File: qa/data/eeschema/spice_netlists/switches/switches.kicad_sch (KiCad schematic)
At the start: 8 parts, among them K1 ADW11

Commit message: Sim: Implement "enum" model parameters for switches
Displayed in Sim Model Dialog parameter grid as a dropdown
(wxEnumProperty).
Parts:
- K1: Sim_Params thr=500m his=0 ron=100m roff=1T ic=on -> thr=500m his=0 ron=100m roff=1T
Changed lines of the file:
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@@
       (effects (font (size 1.27 1.27)) hide)
     )
-    (property "Sim_Params" "thr=500m his=0 ron=100m roff=1T ic=on" (id 7) (at 163.83 83.82 0)
+    (property "Sim_Params" "thr=500m his=0 ron=100m roff=1T" (id 7) (at 163.83 83.82 0)
       (effects (font (size 1.27 1.27)) hide)
     )

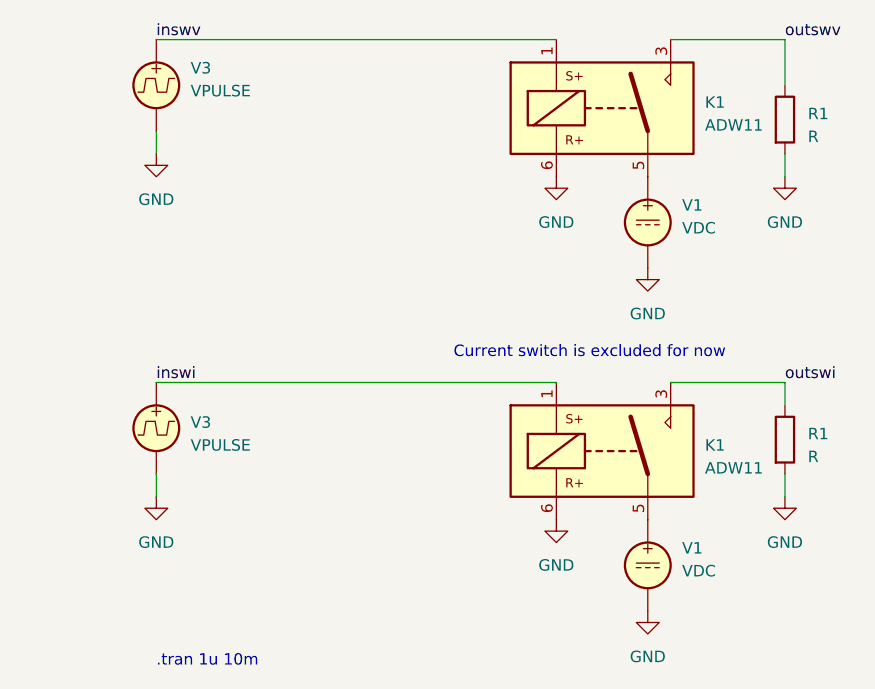
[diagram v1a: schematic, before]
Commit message: Sim: Only store device type in reference, not full model type
Instead of Reference="VSIN1", Value="dc=1 ampl=2 f=3", it's now
Reference="V1", Value="SIN dc=1 ampl=2 f=3".
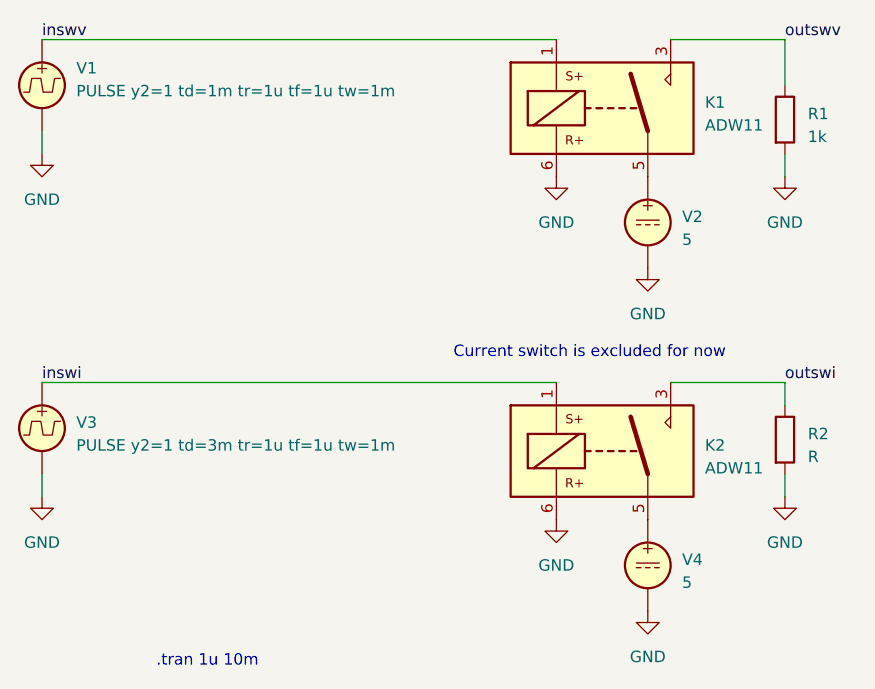
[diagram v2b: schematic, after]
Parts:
- R1: value R -> 1k
- V1: renamed from V3; value VPULSE -> PULSE y2=1 td=1m tr=1u tf=1u tw=1m
- V2, V4: renamed from V1; value VDC -> 5
- V3: value VPULSE -> PULSE y2=1 td=3m tr=1u tf=1u tw=1m; Sim_Device V -> (none); Sim_Disabled 1 -> (none); Sim_Pins 1 2 -> (none); Sim_Type DC -> (none)
- renumbered K1 to K2, R1 to R2
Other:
- moved on the sheet: V1, V3

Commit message: Sim: Rename Sim_Disabled field to Sim_Enable
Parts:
- K2: Sim_Disabled 1 -> (none); Sim_Enable (none) -> 0
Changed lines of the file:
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@@
       (effects (font (size 1.27 1.27)) hide)
     )
-    (property "Sim_Disabled" "1" (at 163.83 121.92 0)
+    (property "Sim_Enable" "0" (at 163.83 121.92 0)
       (effects (font (size 1.27 1.27)) hide)
     )

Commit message: Sim: Remove inference from Reference and Value
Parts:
- removed V3: PULSE y2=1 td=3m tr=1u tf=1u tw=1m, symbol Simulation_SPICE:VPULSE
- added V5: ${SIM_DEVICE} ${SIM_TYPE}, symbol Simulation_SPICE:VPULSE
- R1: Sim_Device (none) -> R
- V1: value PULSE y2=1 td=1m tr=1u tf=1u tw=1m -> ${SIM_DEVICE} ${SIM_TYPE}; Sim_Device (none) -> V; Sim_Params (none) -> y2=1 td=1m tr=1u tf=1u tw=1m; Sim_Type (none) -> PULSE
- V2, V4: Sim_Device (none) -> V
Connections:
- net GND: now also V5.2
- net inswi: now also V5.1
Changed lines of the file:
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@@
   )
   (symbol (lib_id "Simulation_SPICE:VPULSE") (at 101.6 81.28 0) (unit 1)
-    (in_bom yes) (on_board yes) (dnp no) (fields_autoplaced)
+    (in_bom yes) (on_board yes) (dnp no)
     (property "Reference" "V1" (at 105.41 79.375 0)
       (effects (font (size 1.27 1.27)) (justify left))
     )
-    (property "Value" "PULSE y2=1 td=1m tr=1u tf=1u tw=1m" (at 105.41 81.915 0)
+    (property "Value" "${SIM_DEVICE} ${SIM_TYPE}" (at 105.41 81.915 0)
       (effects (font (size 1.27 1.27)) (justify left))
     )
@@
       (effects (font (size 1.27 1.27)) hide)
     )
-    (pin "1")
-    (pin "2")
-    (instances
-      (project "switches"
-        (path "/8c3d4d2c-5107-4b13-88da-bd05d371fd8a"
-          (reference "V1") (unit 1) (value "PULSE y2=1 td=1m tr=1u tf=1u tw=1m") (footprint "")
+    (property "Sim_Device" "V" (at 101.6 81.28 0)
+      (effects (font (size 1.27 1.27)) hide)
+    )
+    (property "Sim_Type" "PULSE" (at 101.6 81.28 0)
+      (effects (font (size 1.27 1.27)) hide)
+    )
+    (property "Sim_Params" "y2=1 td=1m tr=1u tf=1u tw=1m" (at 121.92 83.82 0)
+      (effects (font (size 1.27 1.27)))
+    )
+    (pin "1")
+    (pin "2")
+    (instances
+      (project "switches"
+        (path "/8c3d4d2c-5107-4b13-88da-bd05d371fd8a"
+          (reference "V1") (unit 1) (value "${SIM_DEVICE} ${SIM_TYPE}") (footprint "")
         )
       )
@@
       (effects (font (size 1.27 1.27)) hide)
     )
+    (property "Sim_Device" "V" (at 168.91 96.52 0)
+      (effects (font (size 1.27 1.27)) hide)
+    )
     (pin "1")
     (pin "2")
@@
   (symbol (lib_id "power:GND") (at 158.75 91.44 0) (unit 1)
     (in_bom yes) (on_board yes) (dnp no) (fields_autoplaced)
-    (property "Reference" "#PWR?" (at 158.75 97.79 0)
+    (property "Reference" "#PWR0106" (at 158.75 97.79 0)
       (effects (font (size 1.27 1.27)) hide)
     )
@@
       (project "switches"
         (path "/8c3d4d2c-5107-4b13-88da-bd05d371fd8a"
-          (reference "#PWR?") (unit 1) (value "GND") (footprint "")
-        )
-      )
-    )
-  )
-  (symbol (lib_id "Simulation_SPICE:VPULSE") (at 101.6 119.38 0) (unit 1)
-    (in_bom yes) (on_board yes) (dnp no) (fields_autoplaced)
-    (property "Reference" "V3" (at 105.41 118.745 0)
-      (effects (font (size 1.27 1.27)) (justify left))
-    )
-    (property "Value" "PULSE y2=1 td=3m tr=1u tf=1u tw=1m" (at 105.41 121.285 0)
-      (effects (font (size 1.27 1.27)) (justify left))
-    )
-    (property "Footprint" "" (at 101.6 119.38 0)
-      (effects (font (size 1.27 1.27)) hide)
-    )
-    (property "Datasheet" "~" (at 101.6 119.38 0)
-      (effects (font (size 1.27 1.27)) hide)
-    )
-    (pin "1")
-    (pin "2")
-    (instances
-      (project "switches"
-        (path "/8c3d4d2c-5107-4b13-88da-bd05d371fd8a"
-          (reference "V3") (unit 1) (value "PULSE y2=1 td=3m tr=1u tf=1u tw=1m") (footprint "")
+          (reference "#PWR0106") (unit 1) (value "GND") (footprint "")
         )
       )
@@
   (symbol (lib_id "power:GND") (at 101.6 88.9 0) (unit 1)
     (in_bom yes) (on_board yes) (dnp no) (fields_autoplaced)
-    (property "Reference" "#PWR?" (at 101.6 95.25 0)
+    (property "Reference" "#PWR0104" (at 101.6 95.25 0)
       (effects (font (size 1.27 1.27)) hide)
     )
@@
       (project "switches"
         (path "/8c3d4d2c-5107-4b13-88da-bd05d371fd8a"
-          (reference "#PWR?") (unit 1) (value "GND") (footprint "")
+          (reference "#PWR0104") (unit 1) (value "GND") (footprint "")
         )
       )
@@
   (symbol (lib_id "power:GND") (at 158.75 129.54 0) (unit 1)
     (in_bom yes) (on_board yes) (dnp no) (fields_autoplaced)
-    (property "Reference" "#PWR?" (at 158.75 135.89 0)
+    (property "Reference" "#PWR0103" (at 158.75 135.89 0)
       (effects (font (size 1.27 1.27)) hide)
     )
@@
       (project "switches"
         (path "/8c3d4d2c-5107-4b13-88da-bd05d371fd8a"
-          (reference "#PWR?") (unit 1) (value "GND") (footprint "")
+          (reference "#PWR0103") (unit 1) (value "GND") (footprint "")
         )
       )
@@
   (symbol (lib_id "power:GND") (at 184.15 127 0) (unit 1)
     (in_bom yes) (on_board yes) (dnp no) (fields_autoplaced)
-    (property "Reference" "#PWR?" (at 184.15 133.35 0)
+    (property "Reference" "#PWR0105" (at 184.15 133.35 0)
       (effects (font (size 1.27 1.27)) hide)
     )
@@
       (project "switches"
         (path "/8c3d4d2c-5107-4b13-88da-bd05d371fd8a"
-          (reference "#PWR?") (unit 1) (value "GND") (footprint "")
+          (reference "#PWR0105") (unit 1) (value "GND") (footprint "")
         )
       )
@@
   (symbol (lib_id "power:GND") (at 101.6 127 0) (unit 1)
     (in_bom yes) (on_board yes) (dnp no) (fields_autoplaced)
-    (property "Reference" "#PWR?" (at 101.6 133.35 0)
+    (property "Reference" "#PWR0101" (at 101.6 133.35 0)
       (effects (font (size 1.27 1.27)) hide)
     )
@@
       (project "switches"
         (path "/8c3d4d2c-5107-4b13-88da-bd05d371fd8a"
-          (reference "#PWR?") (unit 1) (value "GND") (footprint "")
+          (reference "#PWR0101") (unit 1) (value "GND") (footprint "")
         )
       )
@@
       (effects (font (size 1.27 1.27)) hide)
     )
+    (property "Sim_Device" "R" (at 184.15 85.09 0)
+      (effects (font (size 1.27 1.27)) hide)
+    )
     (pin "1")
     (pin "2")
@@
   (symbol (lib_id "power:GND") (at 168.91 139.7 0) (unit 1)
     (in_bom yes) (on_board yes) (dnp no) (fields_autoplaced)
-    (property "Reference" "#PWR?" (at 168.91 146.05 0)
+    (property "Reference" "#PWR0102" (at 168.91 146.05 0)
       (effects (font (size 1.27 1.27)) hide)
     )
@@
       (project "switches"
         (path "/8c3d4d2c-5107-4b13-88da-bd05d371fd8a"
-          (reference "#PWR?") (unit 1) (value "GND") (footprint "")
+          (reference "#PWR0102") (unit 1) (value "GND") (footprint "")
         )
       )
@@
     )
   )
+  (symbol (lib_id "Simulation_SPICE:VPULSE") (at 101.6 119.38 0) (unit 1)
+    (in_bom yes) (on_board yes) (dnp no)
+    (property "Reference" "V5" (at 105.41 117.475 0)
+      (effects (font (size 1.27 1.27)) (justify left))
+    )
+    (property "Value" "${SIM_DEVICE} ${SIM_TYPE}" (at 105.41 120.015 0)
+      (effects (font (size 1.27 1.27)) (justify left))
+    )
+    (property "Footprint" "" (at 101.6 119.38 0)
+      (effects (font (size 1.27 1.27)) hide)
+    )
+    (property "Datasheet" "~" (at 101.6 119.38 0)
+      (effects (font (size 1.27 1.27)) hide)
+    )
+    (property "Sim_Device" "V" (at 101.6 119.38 0)
+      (effects (font (size 1.27 1.27)) hide)
+    )
+    (property "Sim_Type" "PULSE" (at 101.6 119.38 0)
+      (effects (font (size 1.27 1.27)) hide)
+    )
+    (property "Sim_Params" "y2=1 td=3m tr=1u tf=1u tw=1m" (at 121.92 121.92 0)
+      (effects (font (size 1.27 1.27)))
+    )
+    (pin "1")
+    (pin "2")
+    (instances
+      (project "switches"
+        (path "/8c3d4d2c-5107-4b13-88da-bd05d371fd8a"
+          (reference "V5") (unit 1) (value "${SIM_DEVICE} ${SIM_TYPE}") (footprint "")
+        )
+      )
+    )
+  )
   (symbol (lib_id "power:GND") (at 168.91 101.6 0) (unit 1)
     (in_bom yes) (on_board yes) (dnp no) (fields_autoplaced)
-    (property "Reference" "#PWR?" (at 168.91 107.95 0)
+    (property "Reference" "#PWR0108" (at 168.91 107.95 0)
       (effects (font (size 1.27 1.27)) hide)
     )
@@
       (project "switches"
         (path "/8c3d4d2c-5107-4b13-88da-bd05d371fd8a"
-          (reference "#PWR?") (unit 1) (value "GND") (footprint "")
+          (reference "#PWR0108") (unit 1) (value "GND") (footprint "")
         )
       )
@@
       (effects (font (size 1.27 1.27)) hide)
     )
+    (property "Sim_Device" "V" (at 168.91 134.62 0)
+      (effects (font (size 1.27 1.27)) hide)
+    )
     (pin "1")
     (pin "2")
@@
   (symbol (lib_id "power:GND") (at 184.15 91.44 0) (unit 1)
     (in_bom yes) (on_board yes) (dnp no) (fields_autoplaced)
-    (property "Reference" "#PWR?" (at 184.15 97.79 0)
+    (property "Reference" "#PWR0107" (at 184.15 97.79 0)
       (effects (font (size 1.27 1.27)) hide)
     )
@@
       (project "switches"
         (path "/8c3d4d2c-5107-4b13-88da-bd05d371fd8a"
-          (reference "#PWR?") (unit 1) (value "GND") (footprint "")
-        )
-      )
+          (reference "#PWR0107") (unit 1) (value "GND") (footprint "")
+        )
+      )

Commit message: Sim: Rename Sim_* fields to Sim.*
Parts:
- K1: Sim_Device SW -> (none); Sim_Params thr=500m his=0 ron=100m roff=1T -> (none); Sim_Pins 1 6 3 5 -> (none); Sim_Type V -> (none)
- K2: Sim_Device SW -> (none); Sim_Enable 0 -> (none); Sim_Pins 1 6 3 5 -> (none); Sim_Type I -> (none)
- R1: Sim_Device R -> (none)
- R2: Sim_Device R -> (none); Sim_Pins 1 2 -> (none)
- V1: value ${SIM_DEVICE} ${SIM_TYPE} -> ${Sim.Device} ${Sim.Type}; Sim_Device V -> (none); Sim_Params y2=1 td=1m tr=1u tf=1u tw=1m -> (none); Sim_Type PULSE -> (none)
- V2, V4: Sim_Device V -> (none)
- V5: value ${SIM_DEVICE} ${SIM_TYPE} -> ${Sim.Device} ${Sim.Type}; Sim_Device V -> (none); Sim_Params y2=1 td=3m tr=1u tf=1u tw=1m -> (none); Sim_Type PULSE -> (none)
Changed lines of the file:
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@@
       (effects (font (size 1.27 1.27)) (justify left))
     )
-    (property "Value" "${SIM_DEVICE} ${SIM_TYPE}" (at 105.41 81.915 0)
+    (property "Value" "${Sim.Device} ${Sim.Type}" (at 105.41 81.915 0)
       (effects (font (size 1.27 1.27)) (justify left))
     )
@@
       (effects (font (size 1.27 1.27)) hide)
     )
-    (property "Sim_Device" "V" (at 101.6 81.28 0)
-      (effects (font (size 1.27 1.27)) hide)
-    )
-    (property "Sim_Type" "PULSE" (at 101.6 81.28 0)
-      (effects (font (size 1.27 1.27)) hide)
-    )
-    (property "Sim_Params" "y2=1 td=1m tr=1u tf=1u tw=1m" (at 121.92 83.82 0)
+    (property "Sim.Device" "V" (at 101.6 81.28 0)
+      (effects (font (size 1.27 1.27)) hide)
+    )
+    (property "Sim.Type" "PULSE" (at 101.6 81.28 0)
+      (effects (font (size 1.27 1.27)) hide)
+    )
+    (property "Sim.Params" "y2=1 td=1m tr=1u tf=1u tw=1m" (at 121.92 83.82 0)
       (effects (font (size 1.27 1.27)))
     )
@@
       (project "switches"
         (path "/8c3d4d2c-5107-4b13-88da-bd05d371fd8a"
-          (reference "V1") (unit 1) (value "${SIM_DEVICE} ${SIM_TYPE}") (footprint "")
+          (reference "V1") (unit 1) (value "${Sim.Device} ${Sim.Type}") (footprint "")
         )
       )
@@
       (effects (font (size 1.27 1.27)) hide)
     )
-    (property "Sim_Device" "V" (at 168.91 96.52 0)
+    (property "Sim.Device" "V" (at 168.91 96.52 0)
       (effects (font (size 1.27 1.27)) hide)
     )
@@
       (effects (font (size 1.27 1.27)) hide)
     )
-    (property "Sim_Device" "SW" (at 163.83 121.92 0)
-      (effects (font (size 1.27 1.27)) hide)
-    )
-    (property "Sim_Type" "I" (at 163.83 121.92 0)
-      (effects (font (size 1.27 1.27)) hide)
-    )
-    (property "Sim_Pins" "1 6 3 5" (at 163.83 121.92 0)
-      (effects (font (size 1.27 1.27)) hide)
-    )
-    (property "Sim_Enable" "0" (at 163.83 121.92 0)
+    (property "Sim.Device" "SW" (at 163.83 121.92 0)
+      (effects (font (size 1.27 1.27)) hide)
+    )
+    (property "Sim.Type" "I" (at 163.83 121.92 0)
+      (effects (font (size 1.27 1.27)) hide)
+    )
+    (property "Sim.Pins" "1 6 3 5" (at 163.83 121.92 0)
+      (effects (font (size 1.27 1.27)) hide)
+    )
+    (property "Sim.Enable" "0" (at 163.83 121.92 0)
       (effects (font (size 1.27 1.27)) hide)
     )
@@
       (effects (font (size 1.27 1.27)) hide)
     )
-    (property "Sim_Device" "R" (at 184.15 85.09 0)
+    (property "Sim.Device" "R" (at 184.15 85.09 0)
       (effects (font (size 1.27 1.27)) hide)
     )
@@
       (effects (font (size 1.27 1.27)) hide)
     )
-    (property "Sim_Device" "SW" (at 163.83 83.82 0)
-      (effects (font (size 1.27 1.27)) hide)
-    )
-    (property "Sim_Type" "V" (at 163.83 83.82 0)
-      (effects (font (size 1.27 1.27)) hide)
-    )
-    (property "Sim_Pins" "1 6 3 5" (at 163.83 83.82 0)
-      (effects (font (size 1.27 1.27)) hide)
-    )
-    (property "Sim_Params" "thr=500m his=0 ron=100m roff=1T" (at 163.83 83.82 0)
+    (property "Sim.Device" "SW" (at 163.83 83.82 0)
+      (effects (font (size 1.27 1.27)) hide)
+    )
+    (property "Sim.Type" "V" (at 163.83 83.82 0)
+      (effects (font (size 1.27 1.27)) hide)
+    )
+    (property "Sim.Pins" "1 6 3 5" (at 163.83 83.82 0)
+      (effects (font (size 1.27 1.27)) hide)
+    )
+    (property "Sim.Params" "thr=500m his=0 ron=100m roff=1T" (at 163.83 83.82 0)
       (effects (font (size 1.27 1.27)) hide)
     )
@@
       (effects (font (size 1.27 1.27)) (justify left))
     )
-    (property "Value" "${SIM_DEVICE} ${SIM_TYPE}" (at 105.41 120.015 0)
+    (property "Value" "${Sim.Device} ${Sim.Type}" (at 105.41 120.015 0)
       (effects (font (size 1.27 1.27)) (justify left))
     )
@@
       (effects (font (size 1.27 1.27)) hide)
     )
-    (property "Sim_Device" "V" (at 101.6 119.38 0)
-      (effects (font (size 1.27 1.27)) hide)
-    )
-    (property "Sim_Type" "PULSE" (at 101.6 119.38 0)
-      (effects (font (size 1.27 1.27)) hide)
-    )
-    (property "Sim_Params" "y2=1 td=3m tr=1u tf=1u tw=1m" (at 121.92 121.92 0)
+    (property "Sim.Device" "V" (at 101.6 119.38 0)
+      (effects (font (size 1.27 1.27)) hide)
+    )
+    (property "Sim.Type" "PULSE" (at 101.6 119.38 0)
+      (effects (font (size 1.27 1.27)) hide)
+    )
+    (property "Sim.Params" "y2=1 td=3m tr=1u tf=1u tw=1m" (at 121.92 121.92 0)
       (effects (font (size 1.27 1.27)))
     )
@@
       (project "switches"
         (path "/8c3d4d2c-5107-4b13-88da-bd05d371fd8a"
-          (reference "V5") (unit 1) (value "${SIM_DEVICE} ${SIM_TYPE}") (footprint "")
+          (reference "V5") (unit 1) (value "${Sim.Device} ${Sim.Type}") (footprint "")
         )
       )
@@
       (effects (font (size 1.27 1.27)) hide)
     )
-    (property "Sim_Device" "R" (at 184.15 120.65 0)
-      (effects (font (size 1.27 1.27)) hide)
-    )
-    (property "Sim_Pins" "1 2" (at 184.15 120.65 0)
+    (property "Sim.Device" "R" (at 184.15 120.65 0)
+      (effects (font (size 1.27 1.27)) hide)
+    )
+    (property "Sim.Pins" "1 2" (at 184.15 120.65 0)
       (effects (font (size 1.27 1.27)) hide)
     )
@@
       (effects (font (size 1.27 1.27)) hide)
     )
-    (property "Sim_Device" "V" (at 168.91 134.62 0)
-      (effects (font (size 1.27 1.27)) hide)
-    )
+    (property "Sim.Device" "V" (at 168.91 134.62 0)
+      (effects (font (size 1.27 1.27)) hide)
+    )
